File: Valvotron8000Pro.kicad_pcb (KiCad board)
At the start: 2 copper layers, 99.7 x 99.9 mm, 143 parts, among them J1 USB_B_Micro, J10 SMA_K2, J11 SMA_K3, J12 Sens. P2, J13 Sens. P3, J14 Servo1, J15 SWD, J16 Servo2, J17 Sens. P1, J18 24V_OUT_TO_BEC, J19 BEC_8V4_IN, J2 Conn_01x02, J3 CAN_OUT, J4 CAN_IN, J5 PWR SUPPLY, J6 PWR_K1, J7 PWR_K2, J8 PWR_K3, J9 SMA_K1, U1 NCP1117-3.3_SOT223, U10 PCA9548APW, U2 W25Q128JVS, U3 RP2040, U4 MCP2515-xST, U5 MCP2551-I-SN, U6 TSR1-2450E, U7 ADS8681IPW, U8 ADS8681IPW, U9 ADS8681IPW, Y1 ABM8-272-T3, Y3 Crystal_GND24

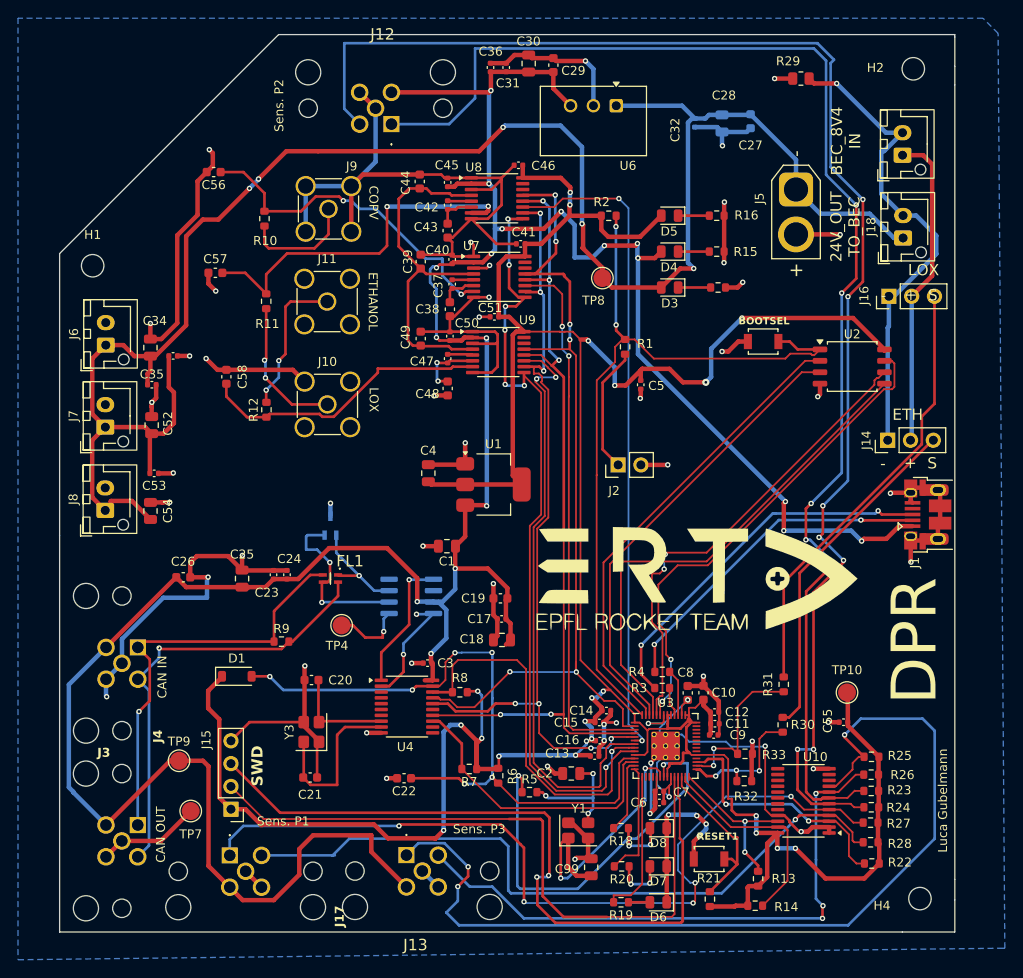
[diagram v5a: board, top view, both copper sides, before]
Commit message: Changement des connecteurs servo (ne tenaient pas le courant en pics (=5A)) ++
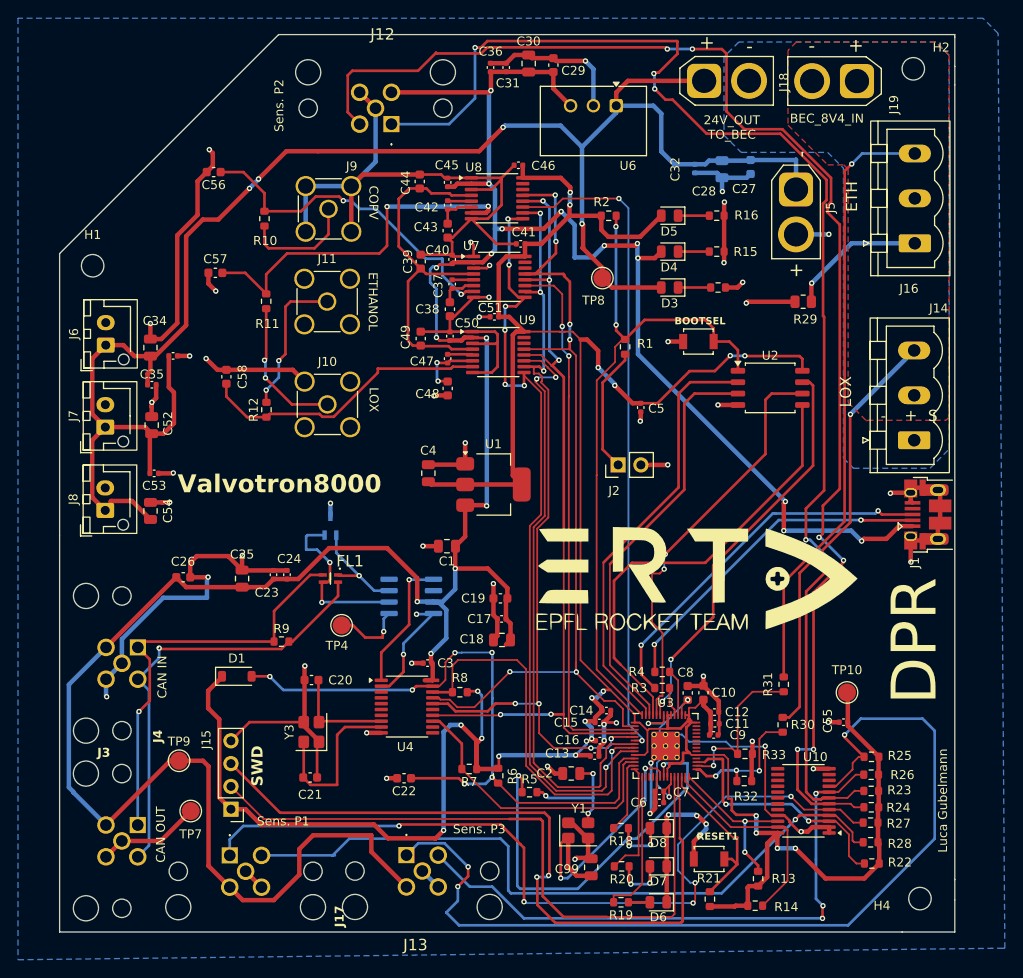
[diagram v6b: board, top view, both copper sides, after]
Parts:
- J14, J16: footprint Connector_PinHeader_2.54mm:PinHeader_1x03_P2.54mm_Vertical -> Connector_Phoenix_MSTB:PhoenixContact_MSTBVA_2,5_3-G_1x03_P5.00mm_Vertical
- J18, J19: footprint Connector_JST:JST_XH_B2B-XH-AM_1x02_P2.50mm_Vertical -> Connector_AMASS:AMASS_XT30U-F_1x02_P5.0mm_Vertical
- moved J18 28.2 mm to (141.3, 48.7), turned to 0 degrees
- moved R29 24.9 mm to (152.3, 73.3)
- moved J19 9.68 mm to (158.3, 48.8), turned to 180 degrees
- moved U2 9.44 mm to (148.7, 82.9)
- moved BOOTSEL1 7.21 mm to (140.7, 77.8)
- moved J16 6.57 mm to (164.8, 66.8)
- moved C27 5.10 mm to (146.5, 58.3)
- moved C28 5.10 mm to (143.3, 58.6)
- moved C32 5.10 mm to (140.3, 58.5)
- moved J14 2.95 mm to (164.7, 88.8)
- moved C5 2.54 mm to (134.2, 85.1)
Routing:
- net GND_SERVO: track 54.2 -> 15.8 mm
- net +8V4_SERVO: track 35.6 -> 0.00 mm
- net Net-(J16-Pin_3): track 49.3 -> 67.8 mm, vias 0 -> 1
- net +24V: track 207.1 -> 191.6 mm, vias 5 -> 4
- net +3V3: track 367.7 -> 353.9 mm
- net /RP2040_integration/QSPI_SS: track 87.8 -> 77.6 mm
- net /RP2040_integration/QSPI_SD3: track 54.8 -> 45.1 mm
- net PTE2_SDA: track 162.6 -> 153.4 mm, vias 7 -> 6
- net Net-(J14-Pin_3): track 38.3 -> 47.4 mm, vias 0 -> 1
- net /RP2040_integration/QSPI_SCLK: track 53.0 -> 46.4 mm
- net /RP2040_integration/QSPI_SD0: track 56.1 -> 49.8 mm
- net /RP2040_integration/QSPI_SD2: track 50.9 -> 46.4 mm
- net /RP2040_integration/QSPI_SD1: track 52.3 -> 48.3 mm
- net PTE2_SCL: track 150.9 -> 148.3 mm
- net GND: track 420.4 -> 421.6 mm
- added copper zone on F.Cu, net +8V4_SERVO
- added copper zone on B.Cu, net GND_SERVO
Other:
- board text added: "BEC_8V4_IN"
- board text added: "Valvotron8000"
- board text removed: "BEC_8V4 IN"

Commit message: Layout done, pcb ready (finally)
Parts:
- removed C17, C24: 10n, Capacitor_SMD:C_0402_1005Metric
- removed C18: 10u, Capacitor_SMD:C_0805_2012Metric
- removed C19: 1u, Capacitor_SMD:C_0603_1608Metric
- removed C3: 100n, Capacitor_SMD:C_0402_1005Metric
- removed TP4: Vref, TestPoint:TestPoint_Pad_D2.0mm
- removed U5: MCP2551-I-SN, Package_SO:SOIC-8_3.9x4.9mm_P1.27mm
- D2: moved to F.Cu
- U4: value MCP2515-xST -> MCP25625x-x-ML; footprint Package_SO:TSSOP-20_4.4x6.5mm_P0.65mm -> Package_DFN_QFN:QFN-28-1EP_6x6mm_P0.65mm_EP4.25x4.25mm
- moved R7 34.2 mm to (94.3, 98.3)
- moved C25 28.6 mm to (114.8, 118.0)
- moved D2 25.2 mm to (111.0, 120.8), turned to -90 degrees
- moved C23 22.1 mm to (113.5, 112.8), turned to -90 degrees
- moved R8 19.5 mm to (103.1, 100.7), turned to 0 degrees
- moved FL1 18.2 mm to (106.1, 121.2), turned to 90 degrees
- moved U4 6.34 mm to (108.6, 112.1)
- moved R9 1.41 mm to (94.3, 109.8), turned to -90 degrees
- renumbered TP8 to 24V, TP10 to 3V3, TP9 to 5V, J2 to BOOT, TP7 to GND
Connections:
- D2 pad 1: Net-(U5-CANH) -> Net-(U4-CANH)
- D2 pad 2: Net-(U5-CANL) -> unconnected-(D2-Pad2)
- FL1 pad 1: Net-(U5-CANH) -> Net-(U4-CANH)
- FL1 pad 3: Net-(U5-CANL) -> unconnected-(D2-Pad2)
- R7 pad 2: INT -> SS
- R8 pad 2: SS -> INT
- U4 pad 1: TXCAN -> SS
- U4 pad 10: GND -> Net-(U4-R_{XD})
- U4 pad 11: unconnected-(U4-~{RX1BF}-Pad11) -> +3.3V
- U4 pad 12: unconnected-(U4-~{RX0BF}-Pad12) -> unconnected-(D2-Pad2)
- U4 pad 13: INT -> Net-(U4-CANH)
- U4 pad 14: SCLK -> unconnected-(U4-NC-Pad14)
- U4 pad 15: unconnected-(U4-NC-Pad15) -> GND
- U4 pad 16: MOSI -> Net-(U4-T_{XD})
- U4 pad 17: MISO -> unconnected-(U4-NC-Pad17)
- U4 pad 18: SS -> GND
- U4 pad 19: RESET_CAN -> +5V
- U4 pad 2: RXCAN -> RESET_CAN
- U4 pad 20: +5V -> Net-(U4-OSC2)
- U4 pad 3: unconnected-(U4-CLKOUT/SOF-Pad3) -> +3.3V
- U4 pad 4: unconnected-(U4-~{TX0RTS}-Pad4) -> Net-(U4-T_{XD})
- U4 pad 5: unconnected-(U4-~{TX1RTS}-Pad5) -> Net-(U4-R_{XD})
- U4 pad 8: Net-(U4-OSC2) -> unconnected-(U4-~{Tx1RTS}-Pad8)
- U4 pad 9: Net-(U4-OSC1) -> unconnected-(U4-~{Tx2RTS}-Pad9)
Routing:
- net SS: track 42.2 -> 79.5 mm, vias 0 -> 8
- net INT: track 32.6 -> 64.0 mm
- net Net-(U4-OSC1): track 19.0 -> 48.3 mm, vias 0 -> 2
- net Net-(U4-OSC2): track 11.7 -> 35.0 mm, vias 0 -> 2
- net Net-(U5-CANL): track 19.5 -> 0.00 mm, vias 2 -> 0
- net Net-(U4-T_{XD}): track 0.00 -> 18.8 mm, vias 0 -> 2
- net MOSI: track 92.5 -> 109.0 mm, vias 7 -> 9
- net TXCAN: track 15.2 -> 0.00 mm, vias 1 -> 0
- net SCLK: track 91.8 -> 105.9 mm, vias 5 -> 7
- net +5V: track 335.1 -> 321.5 mm, vias 18 -> 23
- net MISO: track 99.0 -> 112.3 mm, vias 6 -> 8
- net RXCAN: track 13.1 -> 0.00 mm, vias 2 -> 0
- net unconnected-(D2-Pad2): track 0.00 -> 12.5 mm, vias 0 -> 2
- net +3.3V: track 0.00 -> 12.1 mm
- net Net-(U5-CANH): track 12.0 -> 0.00 mm, vias 1 -> 0
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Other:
- outline, holes or cut-outs redrawn
- board text added: "(La board pas le boug...)"
- board text added: "Flash"
- board text added: "Valvotron8000 Pro-Max"
- board text removed: "BOOTSEL"
- board text removed: "Valvotron8000"
